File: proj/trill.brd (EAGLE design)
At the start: 58.4 x 122.7 mm, 122 parts, among them J1 SPKRAST_01532MR, J2 MICCMA-4544PF-W, J3 ADAFRUIT_OLED_13, J4 DM3D-SFDM, J5 SJ1-3523N, J6 CONUFL001, M1 Z3OC_VIB_MOTOR, U1 SIM5300EA, U10 3.3V 600mA, U11 MCP1642B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

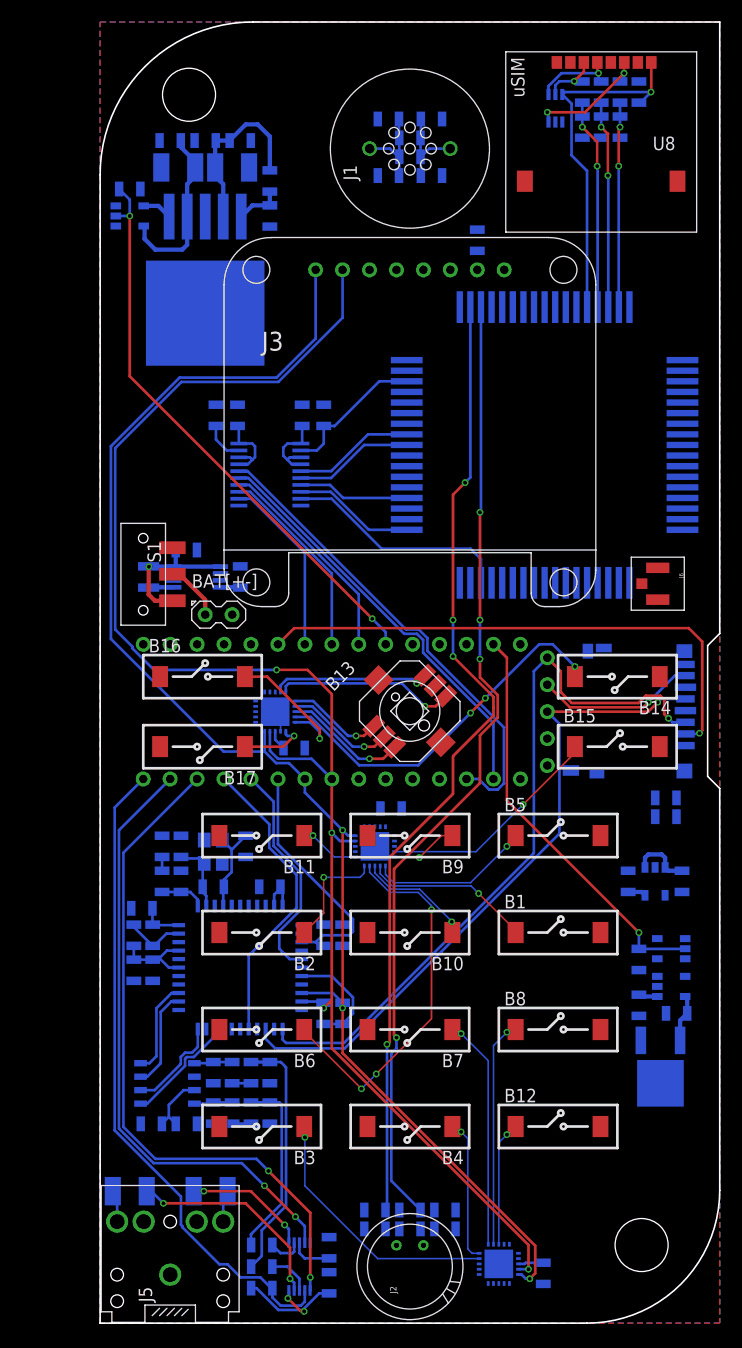
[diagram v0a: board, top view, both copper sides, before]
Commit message: Further routed Trill mobile phone board
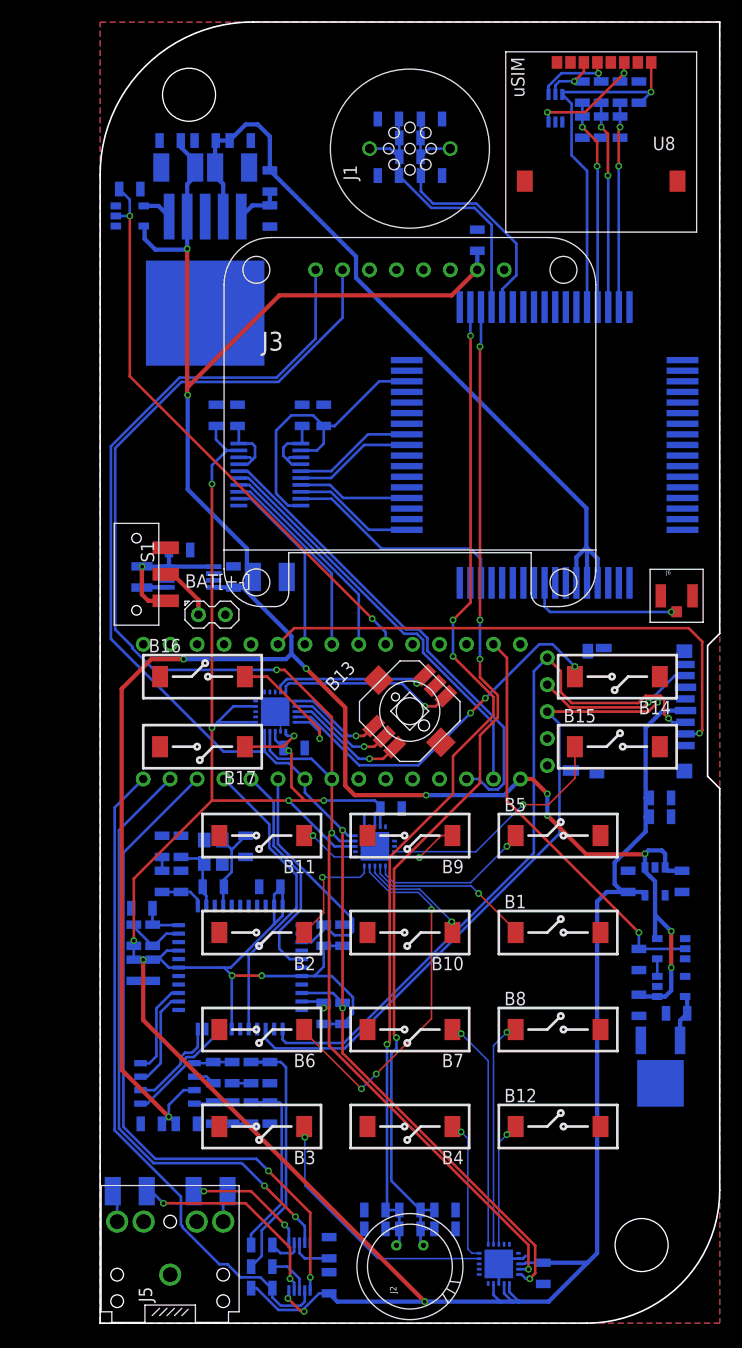
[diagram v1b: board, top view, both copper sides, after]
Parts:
- added C56: 100uF, dooba:1210
- moved J6 2.11 mm to (54.4, 68.6), turned to 0 degrees
- moved C31 1.85 mm to (52.8, 49.5), turned to 180 degrees
- moved C32 1.85 mm to (52.8, 47.8), turned to 180 degrees
- moved L1 0.64 mm to (3.94, 70.4)
- moved S1 0.64 mm to (3.43, 70.6)
- moved BAT[+-] 0.63 mm to (10.5, 66.8)
- moved C25 0.63 mm to (7.49, 72.9)
- moved C26 0.63 mm to (12.6, 70.4)
- moved U11 0.63 mm to (8.51, 70.4)
- turned C38 to 270 degrees
- turned R14 to 270 degrees
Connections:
- net 5.0V: now also C56.1
- net GND: now also C56.2
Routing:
- net 3.3V: track 44.2 -> 311.5 mm, vias 2 -> 12
- net 5.0V: track 31.9 -> 235.1 mm, vias 0 -> 11
- net 3.8V: track 16.9 -> 75.7 mm
- net N$43: track 8.46 -> 27.5 mm
- net N$44: track 8.53 -> 26.9 mm
- net N$61: track 0.00 -> 14.9 mm, vias 0 -> 1
- net N$22: track 13.7 -> 27.9 mm
- net GND: track 2.06 -> 8.80 mm
- net N$47: track 91.6 -> 97.7 mm
- net N$48: track 91.4 -> 97.4 mm
- net N$9: track 21.5 -> 23.4 mm
- net N$62: track 0.00 -> 1.66 mm
- net I2C_SCL: track 149.0 -> 147.4 mm

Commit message: Completed Trill mobile phone board
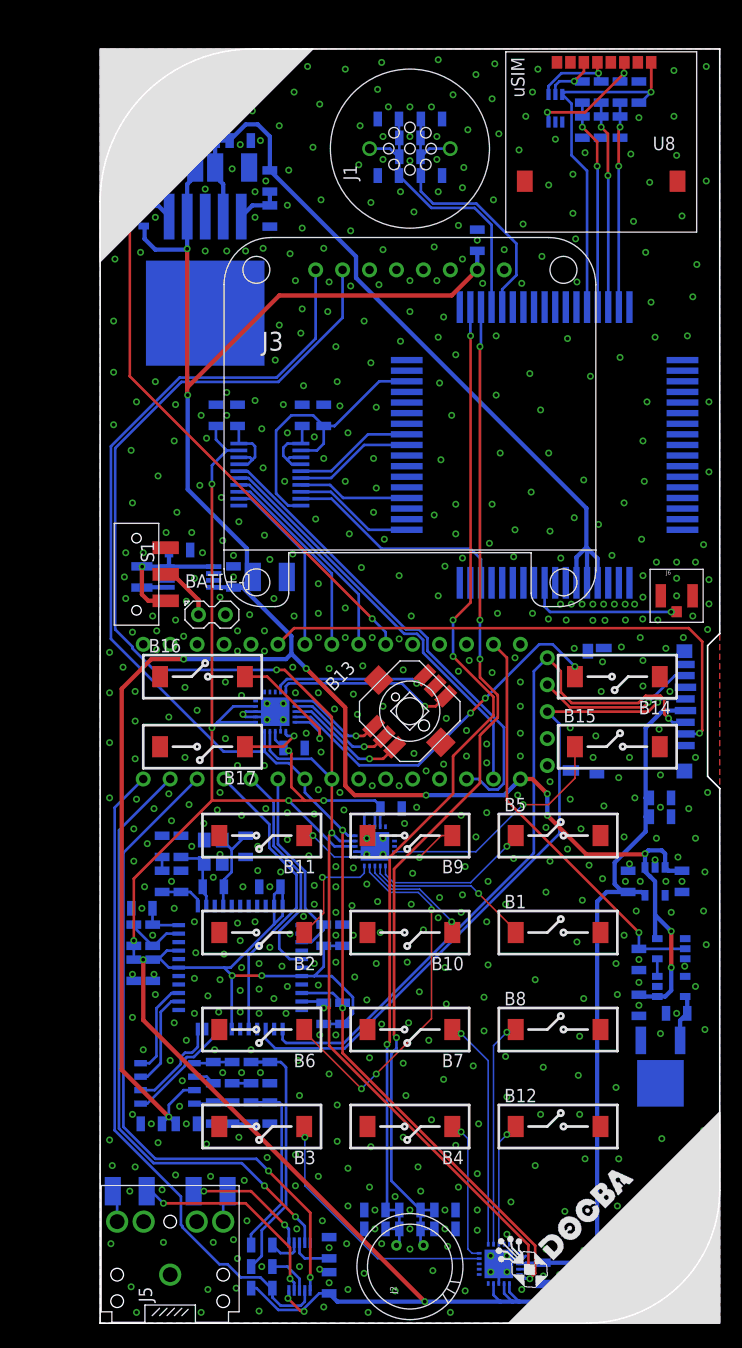
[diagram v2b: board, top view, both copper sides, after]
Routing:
- net GND: track 8.80 -> 17.9 mm, vias 0 -> 622
- net !STA013_RST: track 23.5 -> 18.8 mm
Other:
- board size 58.4 x 122.7 mm -> 58.4 x 120.1 mm
- board text added: "100k"
- board text added: "100nF"
- board text added: "100uF"
- board text added: "10k"
- board text added: "10pF"
- board text added: "10uF"
- board text added: "14.7456 XTAL"
- board text added: "1M"
- board text added: "1k"
- board text added: "1uF"
- board text added: "2.7V"
- board text added: "22pF"
- board text added: "270k"
- board text added: "27pF"
- board text added: "3.3V"
- board text added: "3.3nF"
- board text added: "3.3uF"
- board text added: "33pF"
- board text added: "4.7R"
- board text added: "4.7nF"
- board text added: "4.7uH"
- board text added: "470R"
- board text added: "470pF"
- board text added: "47k"
- board text added: "51R"
- board text added: "560R"
- board text added: "74125"
- board text added: "CS4334"
- board text added: "ESDA6V1"
- board text added: "LM4811"
- board text added: "MCP1642B"
- board text added: "MCP23008"
- board text added: "MIC29302"
- board text added: "MicroSD"
- board text added: "SIM5300EA"
- board text added: "TXB0108"
- board text added: "VIBRATION MOTOR"
- board text added: "ioNode"

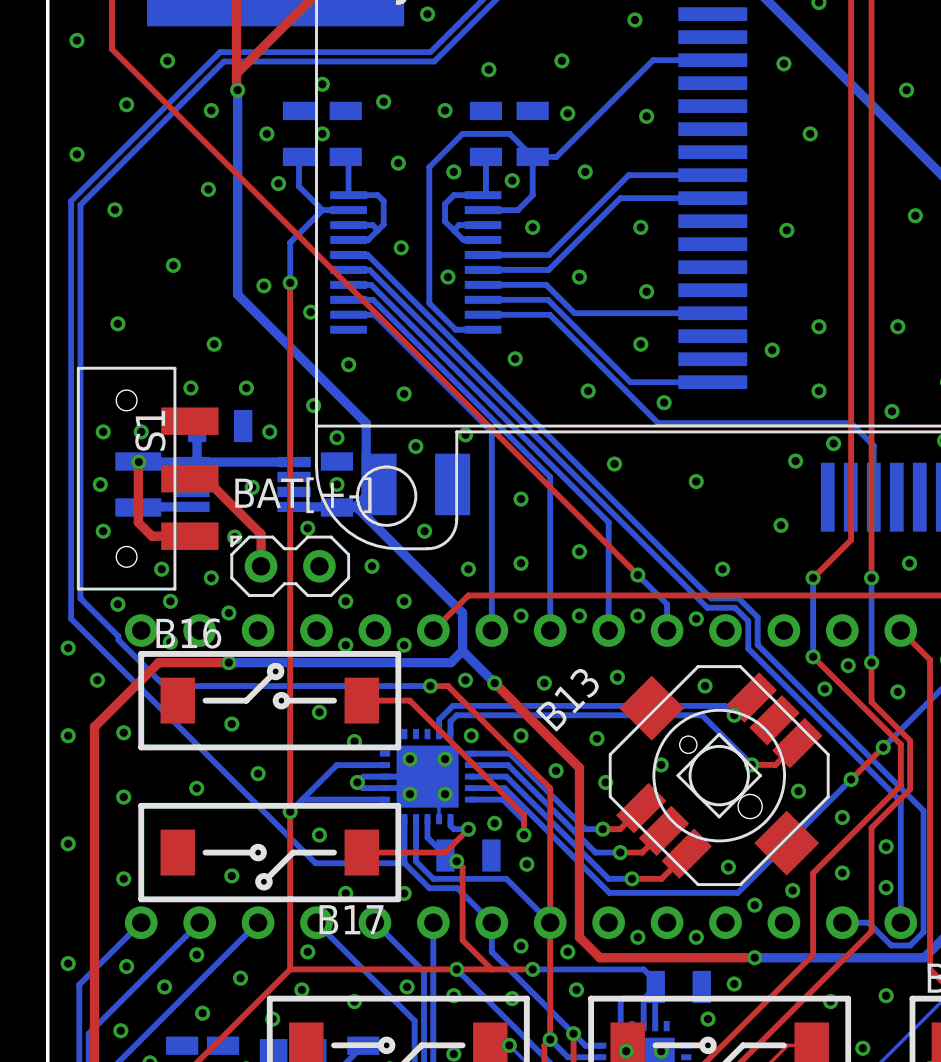
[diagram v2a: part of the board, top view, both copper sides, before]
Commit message: Added 2 LEDs (PWM-able) to Trill Mobile Phone
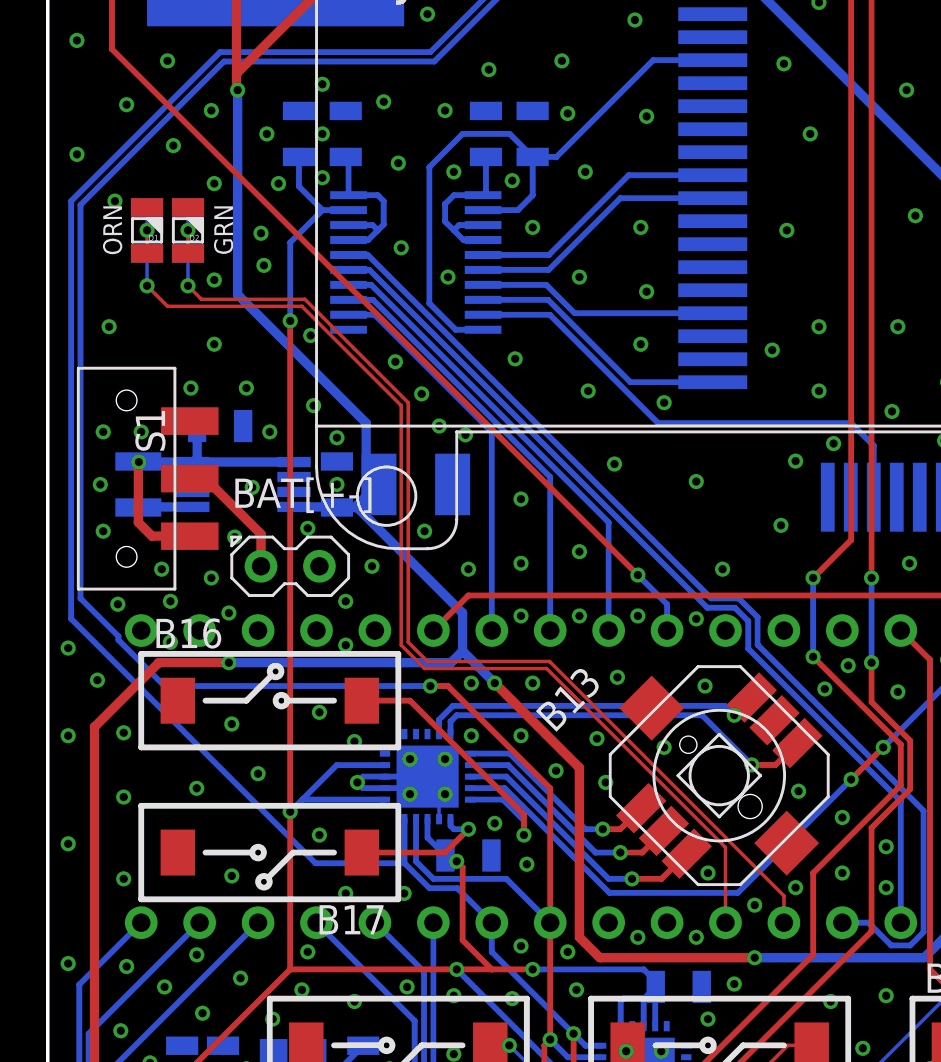
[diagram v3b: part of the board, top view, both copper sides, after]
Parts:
- added D1: GREEN, dooba:0805
- added D2: ORANGE, dooba:0805
- added R21, R24: 1k, dooba:0805
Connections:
- new net N$63: D1.1, R21.2
- new net N$64: D2.1, R24.2
- new net N$65: N1.19, R24.1
- new net N$66: N1.20, R21.1
- net GND: now also D1.2, D2.2
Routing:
- net N$66: track 0.00 -> 46.0 mm, vias 0 -> 1
- net N$65: track 0.00 -> 45.6 mm, vias 0 -> 1
- net N$64: track 0.00 -> 2.00 mm, vias 0 -> 1
- net N$63: track 0.00 -> 2.00 mm, vias 0 -> 1
- net GND: vias 622 -> 623
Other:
- board text added: "GRN"
- board text added: "ORN"
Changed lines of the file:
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@@
 <setting verticaltext="up"/>
 </settings>
-<grid distance="2" unitdist="mil" unit="mil" style="lines" multiple="1" display="yes" altdistance="0.025" altunitdist="inch" altunit="inch"/>
+<grid distance="0.005" unitdist="inch" unit="inch" style="lines" multiple="1" display="yes" altdistance="0.025" altunitdist="inch" altunit="inch"/>
 <layers>
 <layer number="1" name="Top" color="4" fill="1" visible="yes" active="yes"/>
@@
 <rectangle x1="37.46481875" y1="7.874928125" x2="37.82041875" y2="7.925728125" layer="21" rot="R45"/>
 <rectangle x1="37.5305" y1="7.91085" x2="37.6829" y2="7.96165" layer="21" rot="R45"/>
+<text x="4.953" y="83.185" size="0.8128" layer="22" rot="MR0">1k</text>
+<text x="6.731" y="83.185" size="0.8128" layer="22" rot="MR0">1k</text>
+<text x="2.413" y="82.55" size="0.8128" layer="21" rot="R270">ORN</text>
+<text x="7.239" y="82.55" size="0.8128" layer="21" rot="R270">GRN</text>
 </plain>
 <attributes>
@@
 <element name="BAT[+-]" library="dooba" package="PIN_2" value="PIN_2" x="10.541" y="66.802"/>
 <element name="C56" library="dooba" package="1210" value="100uF" x="16.002" y="70.358" rot="MR180"/>
+<element name="D1" library="dooba" package="0805" value="GREEN" x="4.318" y="81.407" rot="R90"/>
+<element name="D2" library="dooba" package="0805" value="ORANGE" x="6.096" y="81.407" rot="R90"/>
+<element name="R21" library="dooba" package="0805" value="1k" x="4.318" y="81.407" rot="MR90"/>
+<element name="R24" library="dooba" package="0805" value="1k" x="6.096" y="81.407" rot="MR90"/>
 </elements>
 <signals>
@@
 <wire x1="41.783" y1="5.699" x2="45.958" y2="5.699" width="0.4064" layer="16"/>
 <wire x1="11.949" y1="82.285" x2="10.541" y2="80.877" width="0.254" layer="16"/>
-<wire x1="10.541" y1="80.877" x2="10.541" y2="79.121" width="0.254" layer="16"/>
-<via x="10.541" y="79.121" extent="1-16" drill="0.3556"/>
+<wire x1="10.541" y1="80.877" x2="10.541" y2="77.47" width="0.254" layer="16"/>
+<via x="10.541" y="77.47" extent="1-16" drill="0.3556"/>
 <wire x1="10.541" y1="49.276" x2="10.541" y2="56.134" width="0.254" layer="1"/>
-<wire x1="10.541" y1="56.134" x2="10.541" y2="79.121" width="0.254" layer="1"/>
+<wire x1="10.541" y1="56.134" x2="10.541" y2="77.47" width="0.254" layer="1"/>
 <wire x1="10.541" y1="49.276" x2="3.175" y2="41.91" width="0.254" layer="1"/>
 <wire x1="3.175" y1="36.068" x2="3.175" y2="41.91" width="0.254" layer="1"/>
@@
 <via x="28.194" y="50.673" extent="1-16" drill="0.3556"/>
 <via x="30.734" y="52.07" extent="1-16" drill="0.3556"/>
-<via x="32.385" y="52.705" extent="1-16" drill="0.3556"/>
-<via x="29.591" y="53.721" extent="1-16" drill="0.3556"/>
+<via x="32.512" y="52.832" extent="1-16" drill="0.3556"/>
+<via x="28.702" y="53.467" extent="1-16" drill="0.3556"/>
 <via x="15.748" y="56.896" extent="1-16" drill="0.3556"/>
 <via x="15.748" y="58.42" extent="1-16" drill="0.3556"/>
@@
 <via x="7.112" y="66.294" extent="1-16" drill="0.3556"/>
 <via x="12.954" y="65.278" extent="1-16" drill="0.3556"/>
-<via x="15.494" y="65.278" extent="1-16" drill="0.3556"/>
 <via x="12.954" y="63.373" extent="1-16" drill="0.3556"/>
-<via x="15.494" y="63.373" extent="1-16" drill="0.3556"/>
 <via x="14.097" y="66.802" extent="1-16" drill="0.3556"/>
 <via x="11.303" y="68.453" extent="1-16" drill="0.3556"/>
@@
 <via x="18.288" y="66.675" extent="1-16" drill="0.3556"/>
 <via x="16.383" y="68.326" extent="1-16" drill="0.3556"/>
-<via x="16.002" y="72.009" extent="1-16" drill="0.3556"/>
+<via x="17.018" y="72.898" extent="1-16" drill="0.3556"/>
 <via x="18.161" y="72.517" extent="1-16" drill="0.3556"/>
 <via x="20.574" y="66.929" extent="1-16" drill="0.3556"/>
@@
 <via x="23.114" y="67.437" extent="1-16" drill="0.3556"/>
 <via x="29.337" y="66.675" extent="1-16" drill="0.3556"/>
-<via x="18.161" y="61.849" extent="1-16" drill="0.3556"/>
+<via x="18.415" y="61.722" extent="1-16" drill="0.3556"/>
 <via x="23.876" y="59.309" extent="1-16" drill="0.3556"/>
-<via x="21.59" y="61.722" extent="1-16" drill="0.3556"/>
+<via x="21.082" y="61.722" extent="1-16" drill="0.3556"/>
 <via x="24.765" y="61.976" extent="1-16" drill="0.3556"/>
 <via x="28.575" y="61.595" extent="1-16" drill="0.3556"/>
-<via x="26.67" y="58.166" extent="1-16" drill="0.3556"/>
+<via x="26.797" y="58.928" extent="1-16" drill="0.3556"/>
 <via x="32.639" y="57.023" extent="1-16" drill="0.3556"/>
 <via x="34.544" y="53.467" extent="1-16" drill="0.3556"/>
@@
 <via x="12.573" y="72.39" extent="1-16" drill="0.3556"/>
 <via x="12.573" y="70.358" extent="1-16" drill="0.3556"/>
-<via x="13.081" y="75.565" extent="1-16" drill="0.3556"/>
-<via x="15.494" y="74.295" extent="1-16" drill="0.3556"/>
+<via x="15.113" y="75.692" extent="1-16" drill="0.3556"/>
+<via x="16.256" y="74.295" extent="1-16" drill="0.3556"/>
 <via x="37.465" y="66.929" extent="1-16" drill="0.3556"/>
 <via x="40.767" y="66.929" extent="1-16" drill="0.3556"/>
@@
 <via x="57.404" y="80.264" extent="1-16" drill="0.3556"/>
 <via x="7.239" y="76.454" extent="1-16" drill="0.3556"/>
-<via x="9.398" y="78.994" extent="1-16" drill="0.3556"/>
-<via x="11.43" y="77.851" extent="1-16" drill="0.3556"/>
+<via x="9.398" y="79.883" extent="1-16" drill="0.3556"/>
+<via x="11.43" y="76.835" extent="1-16" drill="0.3556"/>
 <via x="15.367" y="80.645" extent="1-16" drill="0.3556"/>
 <via x="17.399" y="79.375" extent="1-16" drill="0.3556"/>
@@
 <via x="22.606" y="86.487" extent="1-16" drill="0.3556"/>
 <via x="15.24" y="84.328" extent="1-16" drill="0.3556"/>
-<via x="6.985" y="83.185" extent="1-16" drill="0.3556"/>
-<via x="2.921" y="82.296" extent="1-16" drill="0.3556"/>
-<via x="3.048" y="77.343" extent="1-16" drill="0.3556"/>
-<via x="5.461" y="79.883" extent="1-16" drill="0.3556"/>
+<via x="7.239" y="83.439" extent="1-16" drill="0.3556"/>
+<via x="2.921" y="82.677" extent="1-16" drill="0.3556"/>
+<via x="2.667" y="77.216" extent="1-16" drill="0.3556"/>
+<via x="7.239" y="79.248" extent="1-16" drill="0.3556"/>
 <via x="7.112" y="86.614" extent="1-16" drill="0.3556"/>
 <via x="10.033" y="83.439" extent="1-16" drill="0.3556"/>
@@
 <via x="49.5046" y="67.7926" extent="1-16" drill="0.3556"/>
 <via x="50.3936" y="67.7926" extent="1-16" drill="0.3556"/>
+<contactref element="D1" pad="2"/>
+<contactref element="D2" pad="2"/>
+<via x="9.271" y="81.28" extent="1-16" drill="0.3556"/>
+<via x="5.461" y="85.09" extent="1-16" drill="0.3556"/>
+<via x="11.938" y="83.693" extent="1-16" drill="0.3556"/>
 </signal>
 <signal name="N$28">
@@
 <wire x1="52.533" y1="34.356" x2="52.533" y2="32.7" width="0.254" layer="16"/>
 </signal>
+<signal name="N$63">
+<contactref element="D1" pad="1"/>
+<contactref element="R21" pad="2"/>
+<wire x1="4.318" y1="81.407" x2="4.318" y2="82.407" width="0.1524" layer="16"/>
+<via x="4.318" y="81.407" extent="1-16" drill="0.3556"/>
+<wire x1="4.318" y1="81.407" x2="4.318" y2="80.407" width="0.1524" layer="1"/>
+</signal>
+<signal name="N$64">
+<contactref element="R24" pad="2"/>
+<contactref element="D2" pad="1"/>
+<wire x1="6.096" y1="80.407" x2="6.096" y2="81.407" width="0.1524" layer="1"/>
+<via x="6.096" y="81.407" extent="1-16" drill="0.3556"/>
+<wire x1="6.096" y1="81.407" x2="6.096" y2="82.407" width="0.1524" layer="16"/>
+</signal>
+<signal name="N$65">
+<contactref element="N1" pad="19"/>
+<contactref element="R24" pad="1"/>
+<wire x1="32.004" y1="51.308" x2="32.004" y2="52.4727875" width="0.1524" layer="1"/>
+<wire x1="32.004" y1="52.4727875" x2="21.8149875" y2="62.6618" width="0.1524" layer="1"/>
+<wire x1="21.8149875" y1="62.6618" x2="16.50925625" y2="62.6618" width="0.1524" layer="1"/>
+<wire x1="15.6718" y1="63.49925625" x2="15.6718" y2="73.91325625" width="0.1524" layer="1"/>
+<wire x1="15.6718" y1="73.91325625" x2="11.17525625" y2="78.4098" width="0.1524" layer="1"/>
+<wire x1="16.50925625" y1="62.6618" x2="15.6718" y2="63.49925625" width="0.1524" layer="1"/>
+<wire x1="11.17525625" y1="78.4098" x2="6.6802" y2="78.4098" width="0.1524" layer="1"/>
+<wire x1="6.6802" y1="78.4098" x2="6.096" y2="78.994" width="0.1524" layer="1"/>
+<via x="6.096" y="78.994" extent="1-16" drill="0.3556"/>
+<wire x1="6.096" y1="78.994" x2="6.096" y2="80.407" width="0.1524" layer="16"/>
+</signal>
+<signal name="N$66">
+<contactref element="N1" pad="20"/>
+<contactref element="R21" pad="1"/>
+<wire x1="29.464" y1="51.308" x2="29.464" y2="54.58173125" width="0.1524" layer="1"/>
+<wire x1="21.68873125" y1="62.357" x2="16.383" y2="62.357" width="0.1524" layer="1"/>
+<wire x1="29.464" y1="54.58173125" x2="21.68873125" y2="62.357" width="0.1524" layer="1"/>
+<wire x1="16.383" y1="62.357" x2="15.367" y2="63.373" width="0.1524" layer="1"/>
+<wire x1="15.367" y1="73.787" x2="11.049" y2="78.105" width="0.1524" layer="1"/>
+<wire x1="15.367" y1="63.373" x2="15.367" y2="73.787" width="0.1524" layer="1"/>
+<wire x1="5.207" y1="78.105" x2="4.318" y2="78.994" width="0.1524" layer="1"/>
+<via x="4.318" y="78.994" extent="1-16" drill="0.3556"/>
+<wire x1="4.318" y1="78.994" x2="4.318" y2="80.407" width="0.1524" layer="16"/>
+<wire x1="11.049" y1="78.105" x2="5.207" y2="78.105" width="0.1524" layer="1"/>
+</signal>
 </signals>
